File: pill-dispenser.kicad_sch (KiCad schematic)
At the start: 33 parts, among them J1 USB-C, J2 BAT, J3 Button, J4 WS2812B, J5 Wakeup Button, Q1 AO3401A, Q2 FS8205A, U1 MT3608, U2 ESP32-C3-Zero, U3 TP4056-42-ESOP8, U4 DW01A

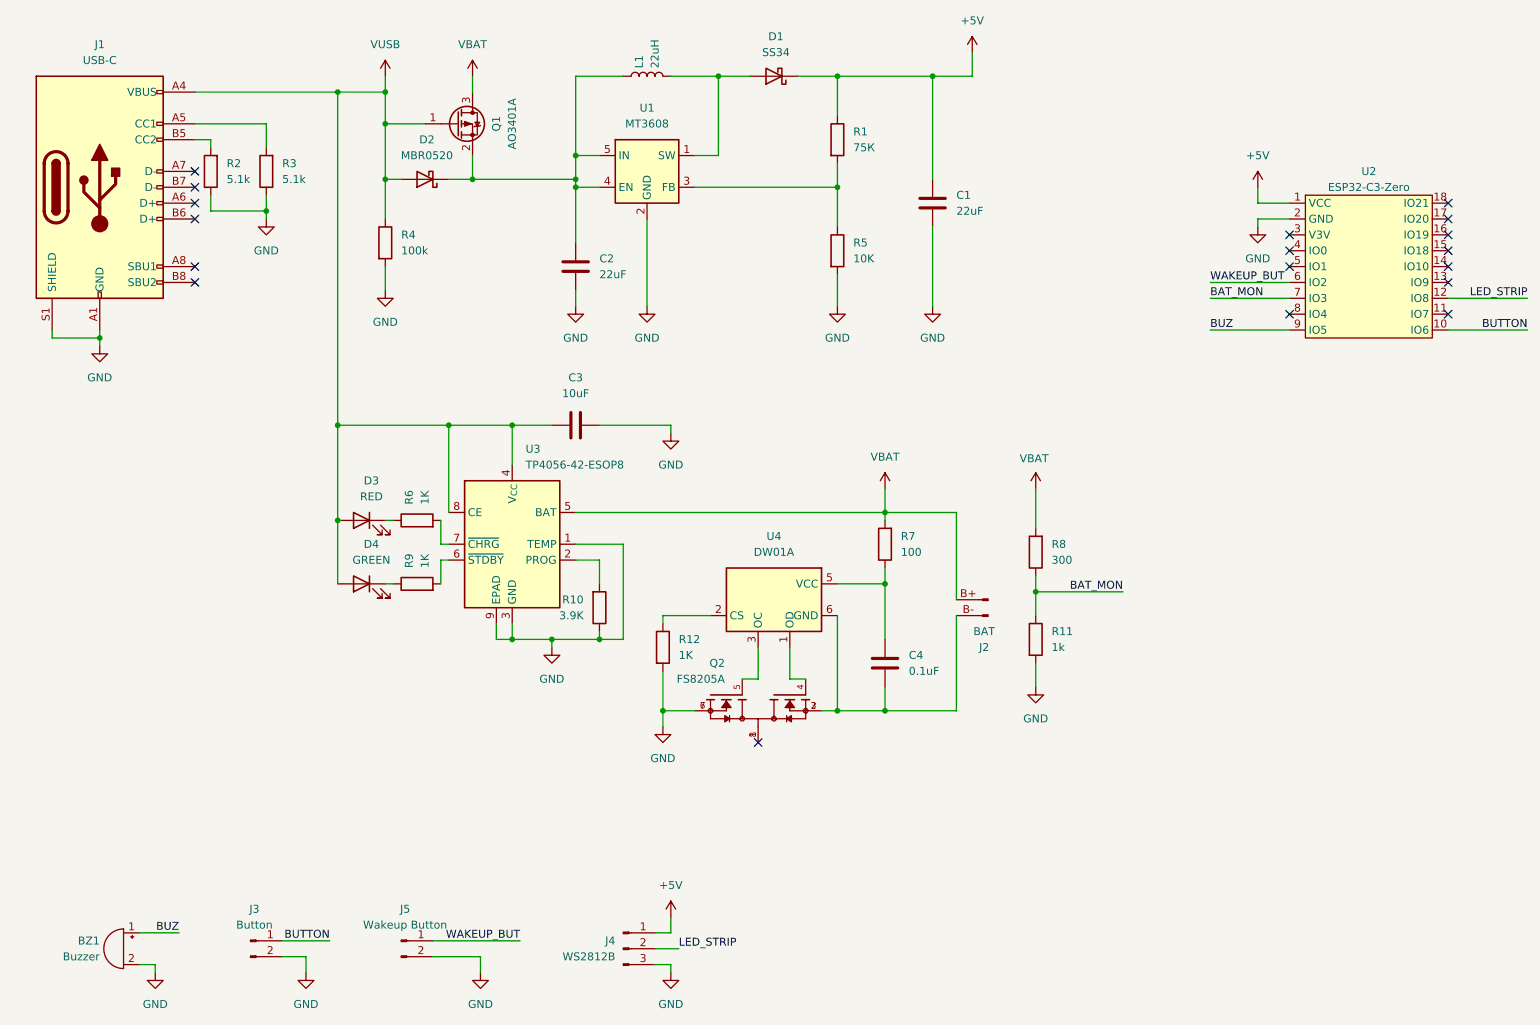
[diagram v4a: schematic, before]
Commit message: Fixed errors in PCB layout
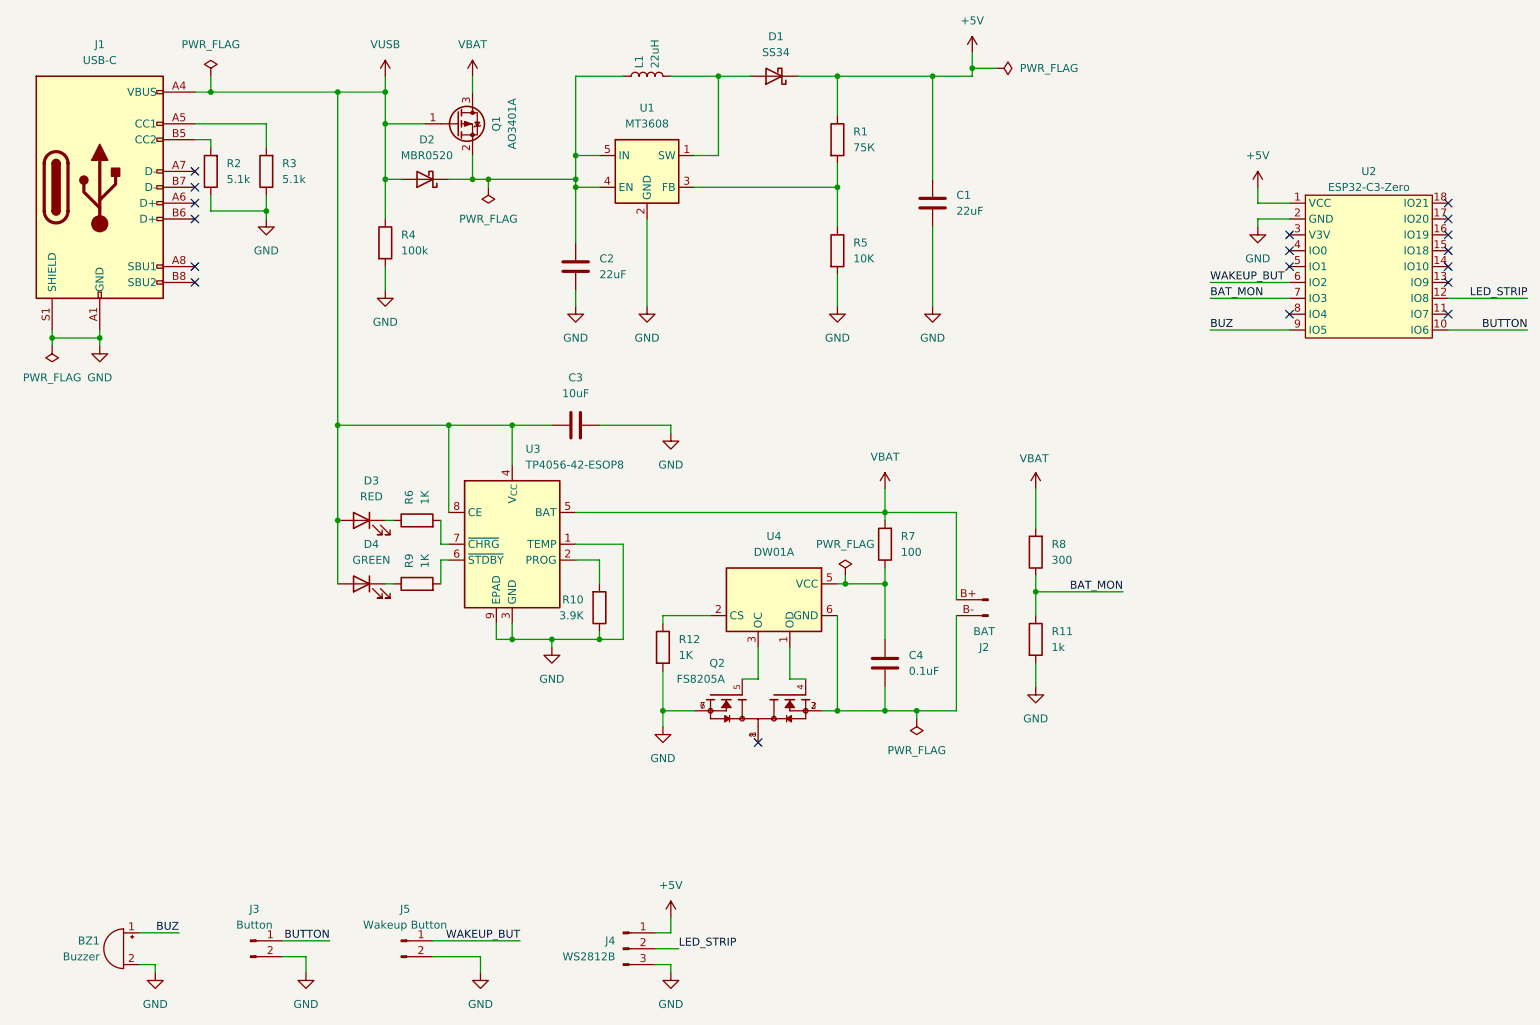
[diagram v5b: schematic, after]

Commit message: Updated PCB to REV1.1 version
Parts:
- removed J2: BAT, Connector_PinSocket_2.54mm:PinSocket_1x02_P2.54mm_Horizontal, symbol Connector:Conn_01x02_Pin
- removed J3: Button, Connector_PinSocket_2.54mm:PinSocket_1x02_P2.54mm_Horizontal, symbol Connector:Conn_01x02_Pin
- removed J4: WS2812B, Connector_PinSocket_2.54mm:PinSocket_1x03_P2.54mm_Horizontal, symbol Connector:Conn_01x03_Pin
- removed J5: Wakeup Button, Connector_PinSocket_2.54mm:PinSocket_1x02_P2.54mm_Horizontal, symbol Connector:Conn_01x02_Pin
- removed U3: TP4056-42-ESOP8, TP4056-42-ESOP8:SOIC127P600X175-9N, symbol Battery_Management:TP4056-42-ESOP8
- added J2: Battery, Connector_PinSocket_2.54mm:PinSocket_1x02_P2.54mm_Horizontal, symbol Connector_Generic:Conn_01x02
- added J3: WS2812B, Connector_PinSocket_2.54mm:PinSocket_1x03_P2.54mm_Horizontal, symbol Connector_Generic:Conn_01x03
- added J4: Button, Connector_PinSocket_2.54mm:PinSocket_1x02_P2.54mm_Horizontal, symbol Connector_Generic:Conn_01x02
- added J5: Wakeup Button, Connector_PinSocket_2.54mm:PinSocket_1x02_P2.54mm_Horizontal, symbol Connector_Generic:Conn_01x02
- added U3: TP4056-42-ESOP8, TP4056-42-ESOP8:SOIC127P600X175-9N, symbol TP4056-42-ESOP8:TP4056-42-ESOP8
- BZ1: footprint Buzzer_Beeper:Indicator_PUI_AI-1440-TWT-24V-2-R -> Buzzer_Beeper:MagneticBuzzer_PUI_AT-0927-TT-6-R; CHIPDIP https://www.chipdip.ru/product/hpm14a -> https://www.chipdip.ru/product0/8307188362
- C3: footprint Capacitor_SMD:C_0805_2012Metric -> Capacitor_SMD:C_1210_3225Metric; CHIPDIP https://www.chipdip.ru/product/grm21br60j106k -> https://www.chipdip.ru/product/grm32dr71e106k
- renumbered D4 to D3, D3 to D4, R9 to R6, R6 to R9
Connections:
- net +5V: now also J3.3 (Pin_3)
- net BUTTON: now also J4.2 (Pin_2)
- net GND: now also J3.1 (Pin_1), J4.1 (Pin_1), J5.1 (Pin_1), U3.1 (TEMP), U3.3 (GND), U3.9 (EXP)
- net LED_STRIP: now also J3.2 (Pin_2)
- net VBAT: now also J2.2 (Pin_2), U3.5 (BAT)
- net VUSB: now also U3.4 (VCC), U3.8 (CE)
- net WAKEUP_BUT: now also J5.2 (Pin_2)
- net at R10.2: now also U3.2 (PROG)
- net at R6.2: now also U3.6 (~{STDBY})
- net at R9.2: now also U3.7 (~{CHRG})
- net at C4.2, Q2.2, Q2.3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: now also J2.1 (Pin_1)
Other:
- moved on the sheet: C3, D3, D4, R10, R6, R9

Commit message: Working on 1.2 final version
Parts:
- removed J2: Battery, Connector_PinSocket_2.54mm:PinSocket_1x02_P2.54mm_Horizontal, symbol Connector_Generic:Conn_01x02
- added BT1: Battery_Cell, Connector_PinHeader_2.54mm:PinHeader_1x02_P2.54mm_Vertical, symbol Device:Battery_Cell
- added SW1: Battery Switch, EG1271:SW_EG1271, symbol EG1271:EG1271
- R11: value 1k -> 75K; CHIPDIP https://www.chipdip.ru/product/1w-2512-1-kom-1 -> https://www.chipdip.ru/product/1w-2512-75-kom-1
- R8: value 300 -> 30K; CHIPDIP https://www.chipdip.ru/product/1w-2512-300-kom-1 -> https://www.chipdip.ru/product0/9001615721
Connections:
- net VBAT: now also SW1.1
- net at C4.2, Q2.2, Q2.3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: now also SW1.4
- new net: BT1.1 (+), SW1.2
- new net: BT1.2 (-), SW1.5
- no-connect marks 18 -> 20
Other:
- company: TelePat, LLC -> I-Pat, LLC
- moved on the sheet: R11, R8

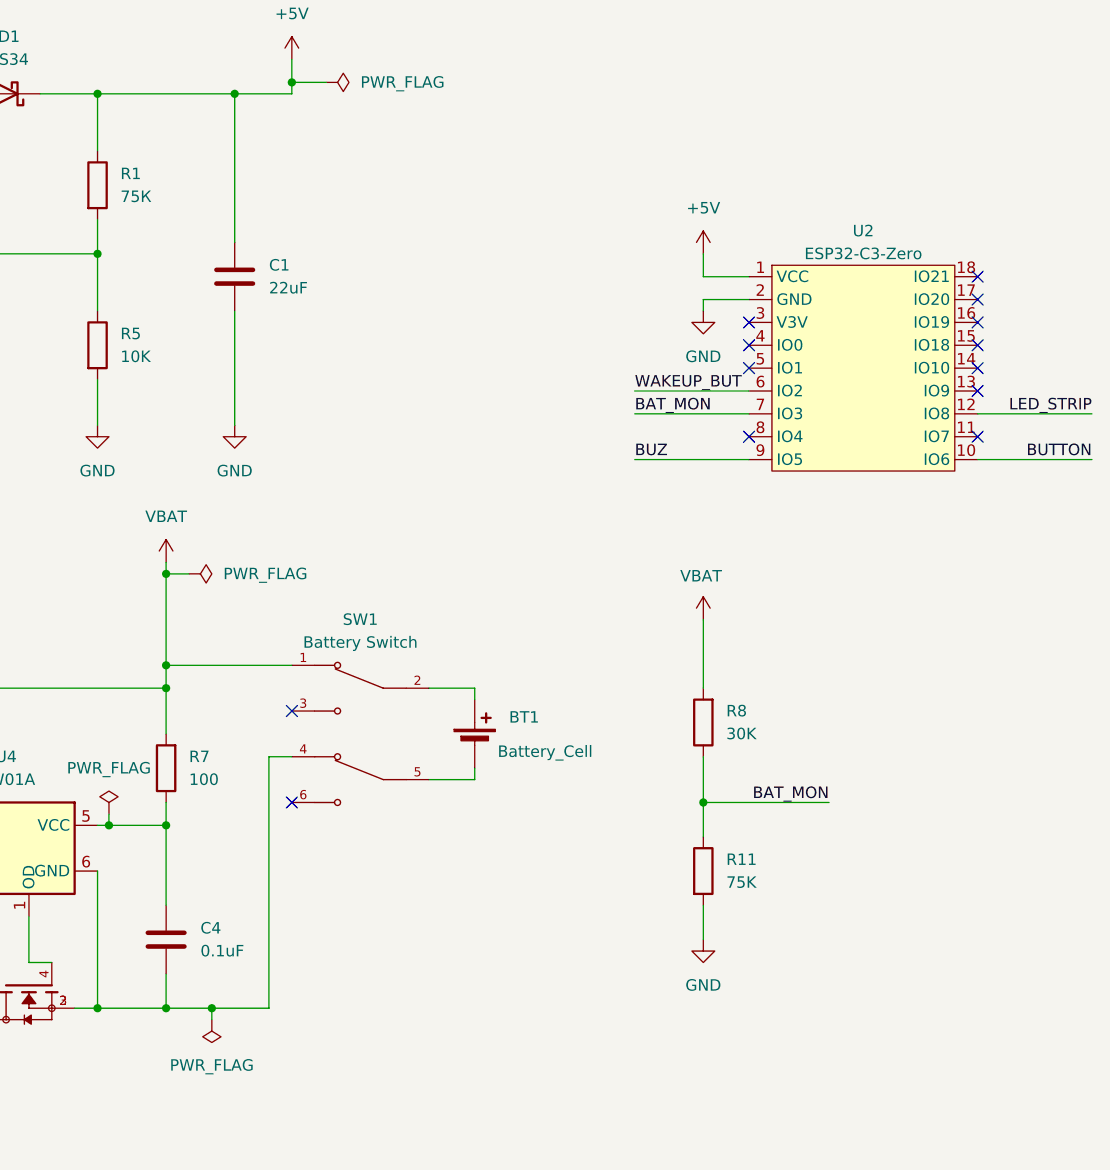
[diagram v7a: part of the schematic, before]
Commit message: Updated pcb to rev1.2
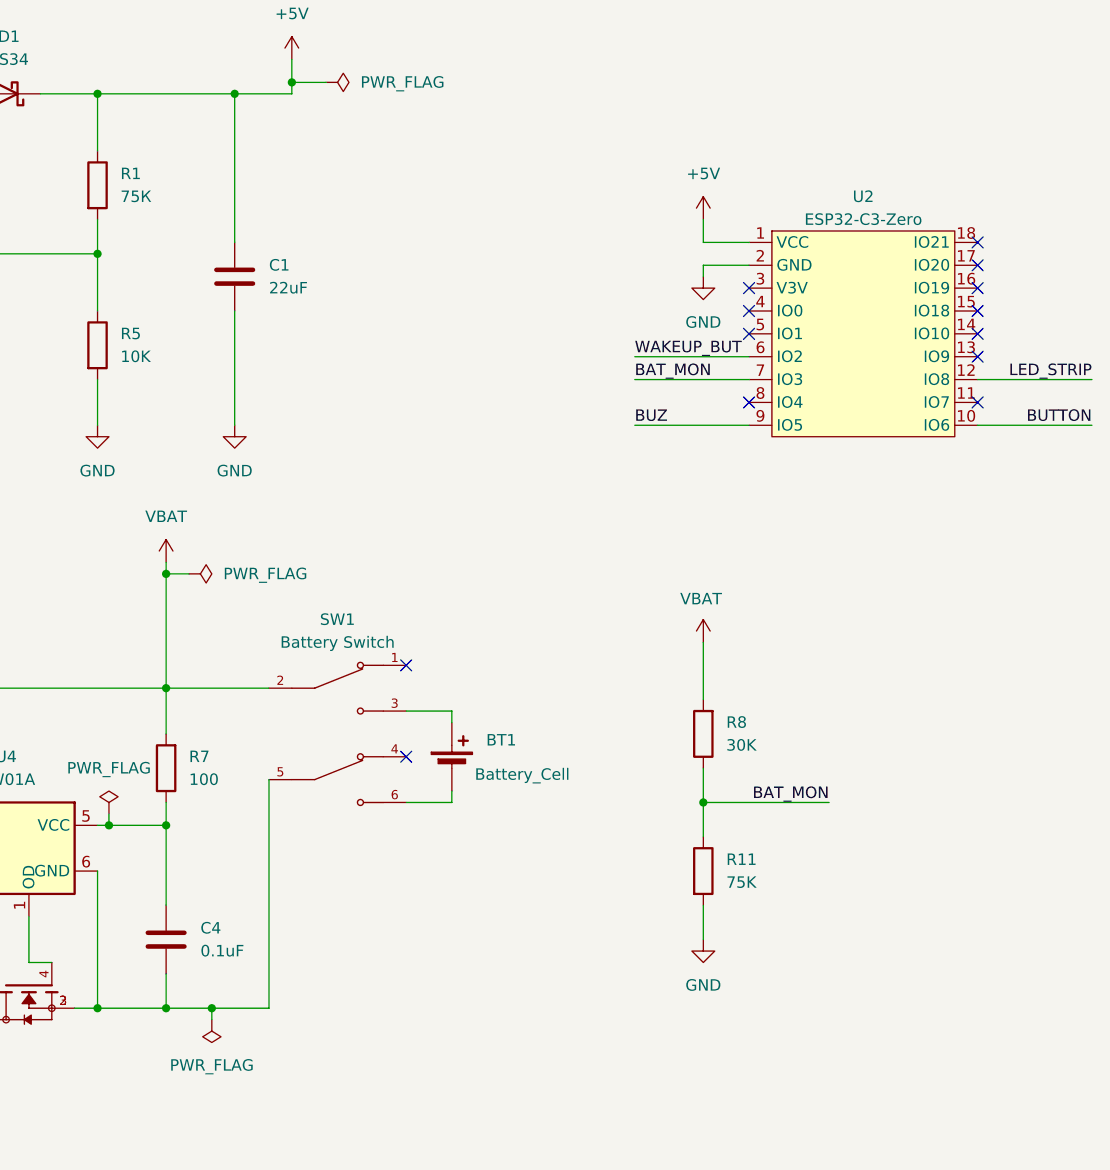
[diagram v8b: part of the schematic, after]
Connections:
- net VBAT: now also SW1.2; no longer SW1.1
- net at C4.2, Q2.2, Q2.3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: now also SW1.5; no longer SW1.4
- net at BT1.1 (+): now also SW1.3; no longer SW1.2
- net at BT1.2 (-): now also SW1.6; no longer SW1.5
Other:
- moved on the sheet: BT1, R8, SW1, U2
